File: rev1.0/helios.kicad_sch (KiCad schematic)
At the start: 56 parts, among them J1 USB_C_Receptacle_USB2.0, J2 helios-pinout, Q1 2N7002VC-, Q2 2N7002VC-, SW1 SWITCH, U1 USBLC6-2P6, U2 TLV75533PDQNR, U3 W25Q128JVPIQ, U4 RP2040, U5 74LVC1T45, Y1 12MHz

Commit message: prod files
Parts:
- D3: JLCPCB_CORRECTION (none) -> 0; 0; 180
- U2: JLCPCB_CORRECTION 0; 0; 270 -> (none)
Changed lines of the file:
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@@
+      (effects (font (size 1.27 1.27)) hide)
+    )
+    (property "JLCPCB_CORRECTION" "0; 0; 180" (id 9) (at 80.01 41.91 0)
       (effects (font (size 1.27 1.27)) hide)
     )
@@
       (effects (font (size 1.27 1.27)) hide)
     )
-    (property "JLCPCB_CORRECTION" "0; 0; 270" (id 9) (at 116.84 44.45 0)
-      (effects (font (size 1.27 1.27)) hide)
-    )

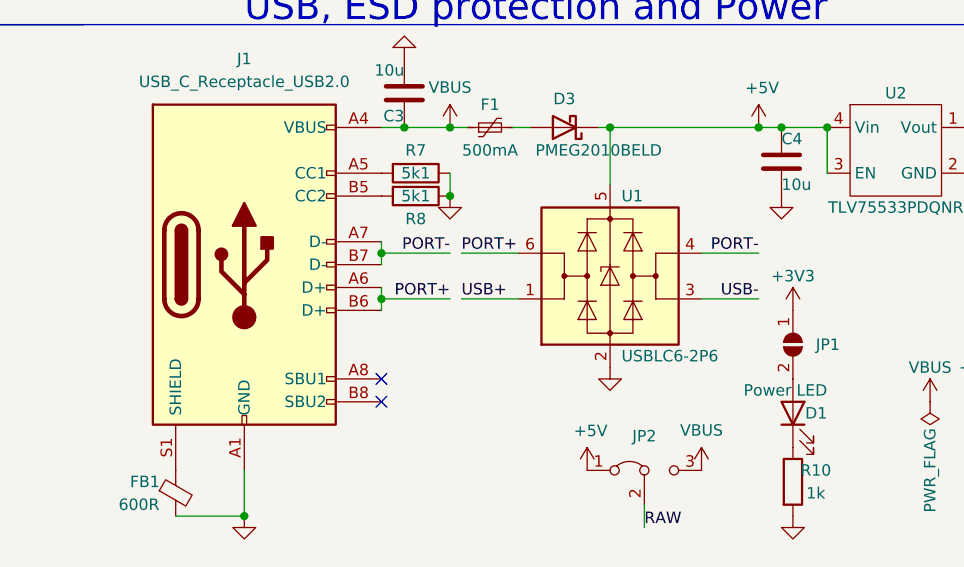
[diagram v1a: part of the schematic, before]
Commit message: widen tabs
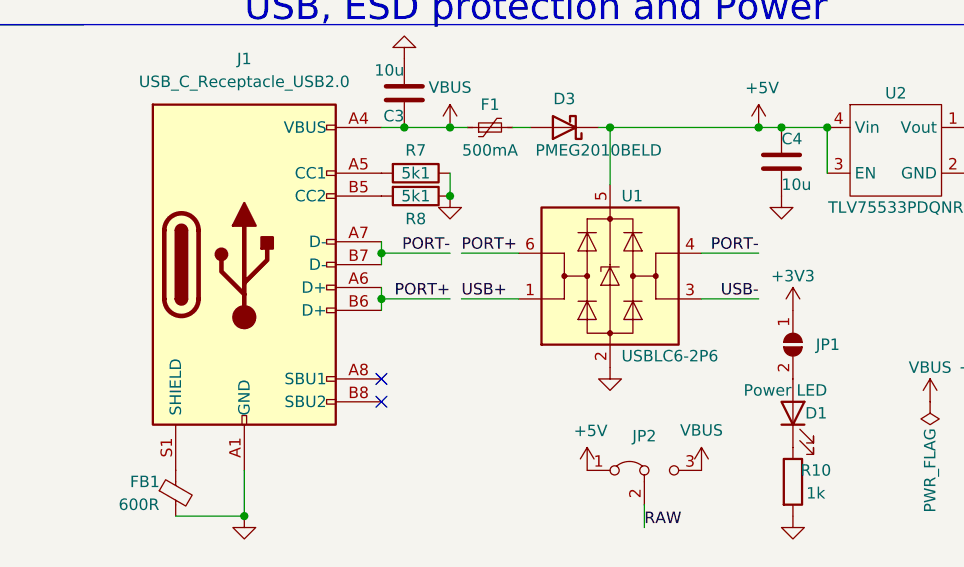
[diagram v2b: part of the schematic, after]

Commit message: manu change
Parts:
- C1: value 4u7 -> 4.7u; JLC Basic Y -> (none); LCSC C23733 -> (none); MPN  CL05A475MP5NRNC -> 4.7uF 20% 10V 0402; Manufacturer Samsung Electro-Mechanics -> (none); Substitute Y -> (none)
- C10, C9: JLC Basic Y -> (none); LCSC C52923 -> (none); MPN  CL05A105KA5NQNC -> 1uF 20% 10V 0402; Manufacturer Samsung Electro-Mechanics -> (none); Substitute Y -> (none)
- C11, C12, C13, C14, C15, C16, C17, C18, C19, C6: JLC Basic Y -> (none); LCSC C1525 -> (none); MPN  CL05B104KO5NNNC -> 100nF 10% 10V 0402; Manufacturer Samsung Electro-Mechanics -> (none); Substitute Y -> (none)
- C2, C3, C4, C5: JLC Basic Y -> (none); LCSC C15525 -> (none); MPN  CL05A106MQ5NUNC -> 10uF 20% 10V 0402; Manufacturer Samsung Electro-Mechanics -> (none); Substitute Y -> (none)
- C7, C8: JLC Basic Y -> (none); LCSC C1548 -> (none); MPN  0402CG150J500NT -> 15pF 5% 10V; Manufacturer FH(Guangdong Fenghua Advanced Tech) -> (none); Substitute Y -> (none)
- D1: JLC Basic N -> (none); LCSC C130719 -> (none); MPN  NCD0402R1 -> B1811URO-20D000113U1930; Manufacturer Foshan-NationStar-Optoelectronics -> (none); Substitute Y -> (none)
- D2: JLC Basic N -> (none); LCSC C130724 -> (none); MPN  NCD0402B1 -> B1811NB--05D000113U1930; Manufacturer Foshan-NationStar-Optoelectronics -> (none); Substitute Y -> (none)
- D3: JLC Basic N -> (none); JLCPCB_CORRECTION 0; 0; 180 -> (none); LCSC C552820 -> (none); Manufacturer Nexperia -> (none); Substitute N -> (none)
- F1: JLC Basic N -> (none); LCSC C210357 -> (none); Manufacturer BOURNS -> (none); Substitute Y -> (none)
- FB1: JLC Basic N -> (none); LCSC C160977 -> (none); Manufacturer Murata Electronics -> (none); Substitute Y -> (none)
- J1: JLC Basic N -> (none); LCSC C963373 -> (none); MPN  GT-USB-7014C -> USB4510-03-1-A; Manufacturer G-Switch -> (none); Substitute N -> (none)
- JP2: now left out of the parts list
- Q1, Q2: JLC Basic N -> (none); JLCPCB_CORRECTION 0; 0; 180 -> (none); LCSC C504145 -> (none); MPN  2N7002V -> 2N7002VC; Manufacturer Diodes Incorporated -> (none); Substitute Y -> (none)
- R1, R11, R17, R2, R3: JLC Basic Y -> (none); LCSC C25744 -> (none); MPN  0402WGF1002TCE -> 10k 1% 0402; Manufacturer UNI-ROYAL(Uniroyal Elec) -> (none); Substitute Y -> (none)
- R10, R14, R15: JLC Basic Y -> (none); LCSC C11702 -> (none); MPN  0402WGF1001TCE -> 1k 1% 0402; Manufacturer UNI-ROYAL(Uniroyal Elec) -> (none); Substitute Y -> (none)
- R12, R13: value 27R -> 27; JLC Basic N -> (none); LCSC C25100 -> (none); MPN  0402WGF270JTCE -> 27 1% 0402; Manufacturer UNI-ROYAL(Uniroyal Elec) -> (none); Substitute Y -> (none)
- R16, R7, R8: value 5k1 -> 5.1k; JLC Basic Y -> (none); LCSC C25905 -> (none); MPN  0402WGF5101TCE -> 5.1k 1% 0402; Manufacturer UNI-ROYAL(Uniroyal Elec) -> (none); Substitute Y -> (none)
- R4, R5, R6: value 51K -> 51k; JLC Basic Y -> (none); LCSC C25794 -> (none); MPN  0402WGF5102TCE -> 51k 1% 0402; Manufacturer UNI-ROYAL(Uniroyal Elec) -> (none); Substitute Y -> (none)
- R9: value 1K -> 1k; JLC Basic Y -> (none); LCSC C11702 -> (none); MPN  0402WGF1001TCE -> 1k 1% 0402; Manufacturer UNI-ROYAL(Uniroyal Elec) -> (none); Substitute Y -> (none)
- SW1: JLC Basic N -> (none); LCSC C589221 -> (none); MPN  ST-1194 -> EVP-BL2A1B000; Manufacturer RI SHENG -> (none); Substitute N -> (none)
- U1: JLC Basic N -> (none); JLCPCB_CORRECTION 0; 0; 270 -> (none); LCSC C2827693 -> (none); Manufacturer TECH PUBLIC -> (none); Substitute N -> (none)
- U2: JLC Basic N -> (none); LCSC C2861882 -> (none); Manufacturer Texas Instruments -> (none); Substitute N -> (none)
- U3: JLC Basic N -> (none); JLCPCB_CORRECTION 0; 0; 270 -> (none); LCSC C190862 -> (none); Manufacturer Winbond -> (none); Substitute N -> (none)
- U4: JLC Basic N -> (none); LCSC C2040 -> (none); MPN  RP2040 -> SC0914(13); Manufacturer Raspberry Pi -> (none); Substitute N -> (none)
- U5: JLC Basic N -> (none); JLCPCB_CORRECTION 0; 0; 270 -> (none); LCSC C352970 -> (none); Manufacturer Texas Instruments -> (none); Substitute N -> (none)
- Y1: JLC Basic N -> (none); LCSC C2149204 -> (none); MPN  2TJ412000HYGBC -> ECS-120-10-36B-CWY-TR3; Manufacturer JYJE -> (none); Substitute N -> (none)

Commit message: Fix readme and add current prod
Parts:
- C1: LCSC (none) -> C23733
- C10, C9: LCSC (none) -> C52923
- C11, C12, C13, C14, C15, C16, C17, C18, C19, C6: LCSC (none) -> C1525
- C2, C3, C4, C5: LCSC (none) -> C15525
- C7, C8: LCSC (none) -> C1548
- D1: LCSC (none) -> C130719
- D2: LCSC (none) -> C130724
- D3: JLCPCB_CORRECTION (none) -> 0; 0; 180; LCSC (none) -> C552820
- F1: LCSC (none) -> C210357
- FB1: LCSC (none) -> C160977
- J1: LCSC (none) -> C963373
- Q1, Q2: JLCPCB_CORRECTION (none) -> 0; 0; 180; LCSC (none) -> C504145
- R1, R11, R17, R2, R3: LCSC (none) -> C25744
- R10, R14, R15, R9: LCSC (none) -> C11702
- R12, R13: LCSC (none) -> C25100
- R16, R7, R8: LCSC (none) -> C25905
- R4, R5, R6: LCSC (none) -> C25794
- SW1: LCSC (none) -> C589221
- U1: JLCPCB_CORRECTION (none) -> 0; 0; 270; LCSC (none) -> C2827693
- U2: LCSC (none) -> C2861882
- U3: JLCPCB_CORRECTION (none) -> 0; 0; 270; LCSC (none) -> C190862
- U4: LCSC (none) -> C2040
- U5: JLCPCB_CORRECTION (none) -> 0; 0; 270; LCSC (none) -> C352970
- Y1: LCSC (none) -> C2149204
